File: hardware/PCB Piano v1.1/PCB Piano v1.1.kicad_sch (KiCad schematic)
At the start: 0 parts

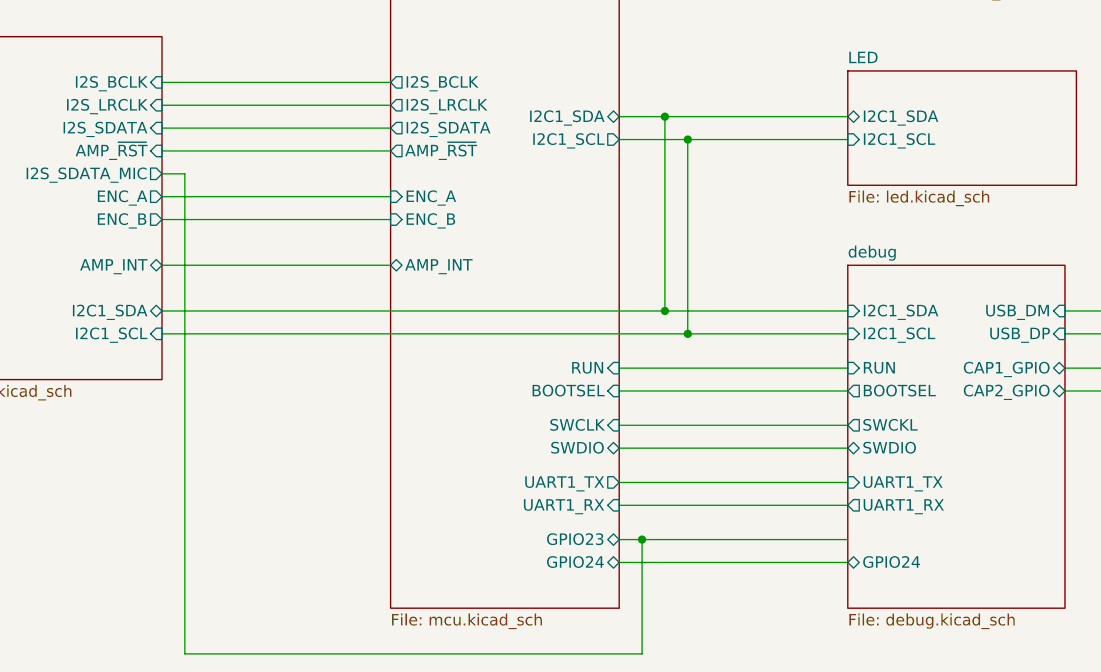
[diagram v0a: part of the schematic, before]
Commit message: Development Phase - PCB Complete - ERC/DRC in progress
Development commit. PBC layout complete. ERC/DRC checks in progress. Swapped some connectors for JST connectors with Adafruit-style polarization.
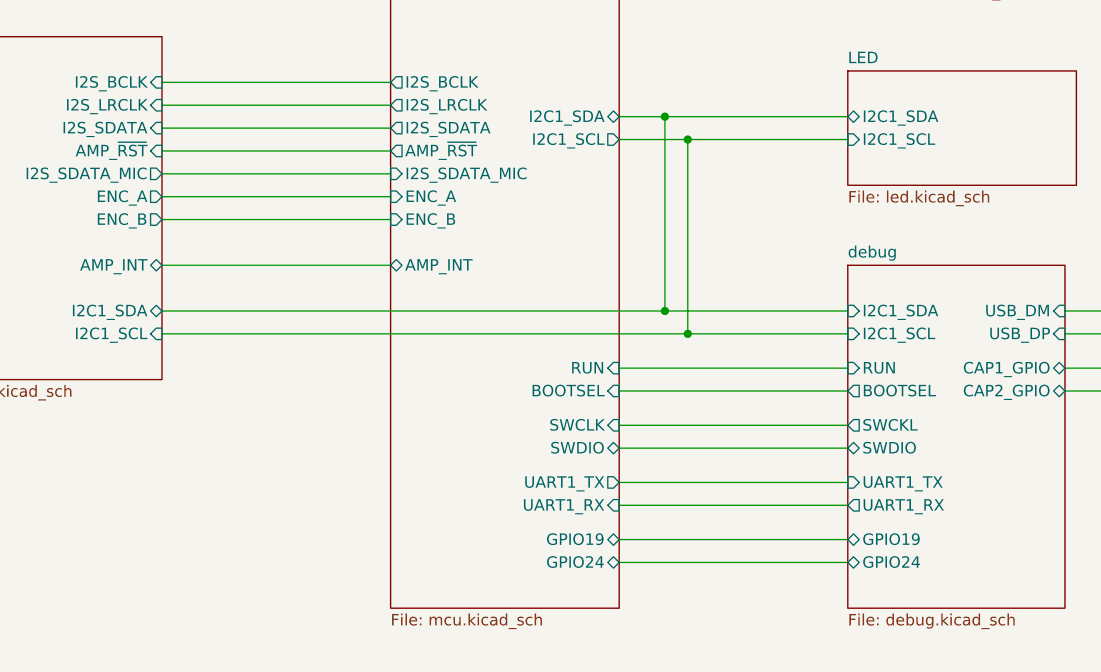
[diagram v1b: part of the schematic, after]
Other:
- sheet MCU ports: added GPIO19, I2S_SDATA_MIC; removed GPIO23
- sheet debug ports: added GPIO19; removed none
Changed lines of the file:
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@@
 		(color 0 0 0 0)
 	)
-	(junction
-		(at 154.94 151.13)
-		(diameter 0)
-		(color 0 0 0 0)
-	)
 	(wire
 		(pts
@@
 	(wire
 		(pts
-			(xy 104.14 163.83) (xy 104.14 110.49)
-		)
-		(stroke
-			(width 0)
-			(type default)
-		)
-	)
-	(wire
-		(pts
 			(xy 101.6 82.55) (xy 127 82.55)
 		)
@@
 	(wire
 		(pts
-			(xy 154.94 151.13) (xy 177.8 151.13)
+			(xy 152.4 151.13) (xy 177.8 151.13)
 		)
 		(stroke
@@
 	(wire
 		(pts
-			(xy 154.94 163.83) (xy 104.14 163.83)
-		)
-		(stroke
-			(width 0)
-			(type default)
-		)
-	)
-	(wire
-		(pts
 			(xy 101.6 64.77) (xy 121.92 64.77)
 		)
@@
 	(wire
 		(pts
-			(xy 152.4 151.13) (xy 154.94 151.13)
-		)
-		(stroke
-			(width 0)
-			(type default)
-		)
-	)
-	(wire
-		(pts
 			(xy 152.4 64.77) (xy 177.8 64.77)
 		)
@@
 	(wire
 		(pts
-			(xy 154.94 151.13) (xy 154.94 163.83)
-		)
-		(stroke
-			(width 0)
-			(type default)
-		)
-	)
-	(wire
-		(pts
 			(xy 207.01 132.08) (xy 207.01 73.66)
 		)
@@
 	(wire
 		(pts
-			(xy 104.14 110.49) (xy 101.6 110.49)
-		)
-		(stroke
-			(width 0)
-			(type default)
-		)
-	)
-	(wire
-		(pts
 			(xy 212.09 125.73) (xy 212.09 48.26)
 		)
@@
 		(pts
 			(xy 208.28 134.62) (xy 201.93 134.62)
+		)
+		(stroke
+			(width 0)
+			(type default)
+		)
+	)
+	(wire
+		(pts
+			(xy 101.6 110.49) (xy 127 110.49)
 		)
 		(stroke
@@
 			)
 		)
+		(pin "GPIO19" bidirectional
+			(at 177.8 151.13 180)
+			(effects
+				(font
+					(size 1.27 1.27)
+				)
+				(justify left)
+			)
+		)
 		(instances
 			(project "PCB Piano v1.1"
@@
 			)
 		)
-		(pin "GPIO23" bidirectional
-			(at 152.4 151.13 0)
-			(effects
-				(font
-					(size 1.27 1.27)
-				)
-				(justify right)
-			)
-		)
 		(pin "BOOTSEL" input
 			(at 152.4 134.62 0)
@@
 			)
 		)
+		(pin "GPIO19" bidirectional
+			(at 152.4 151.13 0)
+			(effects
+				(font
+					(size 1.27 1.27)
+				)
+				(justify right)
+			)
+		)
+		(pin "I2S_SDATA_MIC" input
+			(at 127 110.49 180)
+			(effects
+				(font
+					(size 1.27 1.27)
+				)
+				(justify left)
+			)
+		)

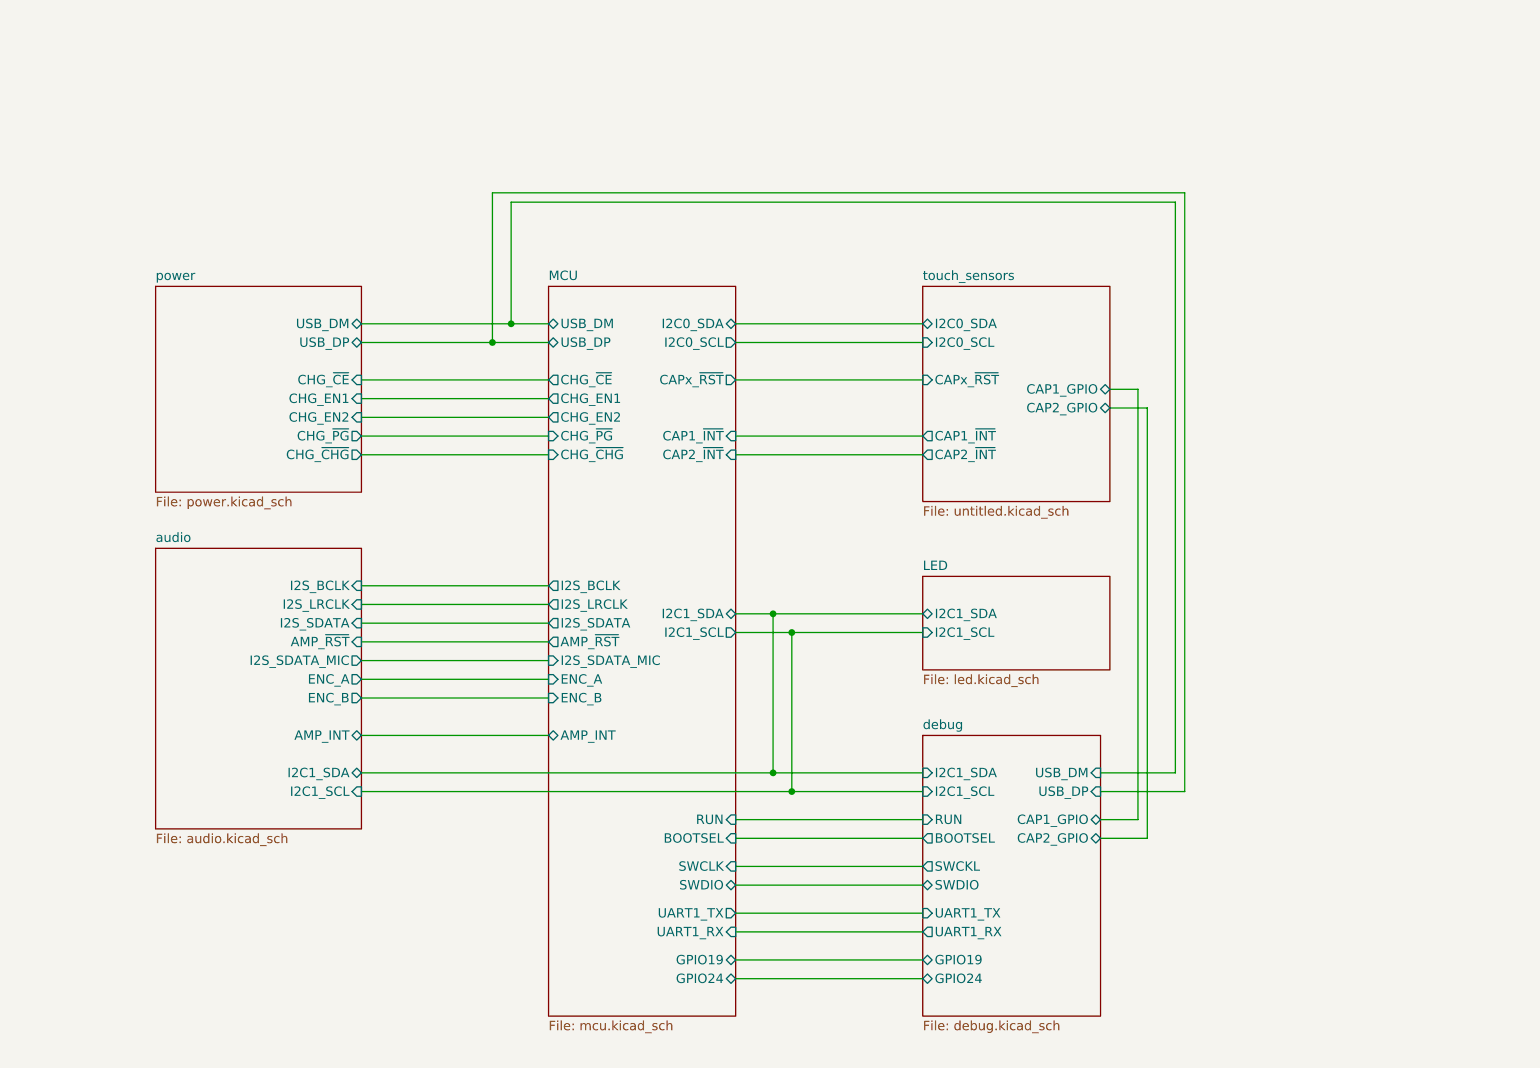
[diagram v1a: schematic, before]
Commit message: Firmware architecture complete - PCB revision with new charger.
Firmware Architecture Complete

- Added MP2724 charger driver
- Added TLV320DAC3100 driver
- Added MTCH2120 touch driver
- Added PCA9685 driver
- Added DotStar driver
- Added rotary encoder driver
- Added touch and LED maps
- Added control/audio/voice managers
- Added audio command queue
- Added Core1 audio architecture
- Added status LED system
- Added LED animation framework

Changes hardware schematic and PCB to accommodate a newer-style USB-C sink battery charger chip and USB data MUX to protect MCU while powered off.
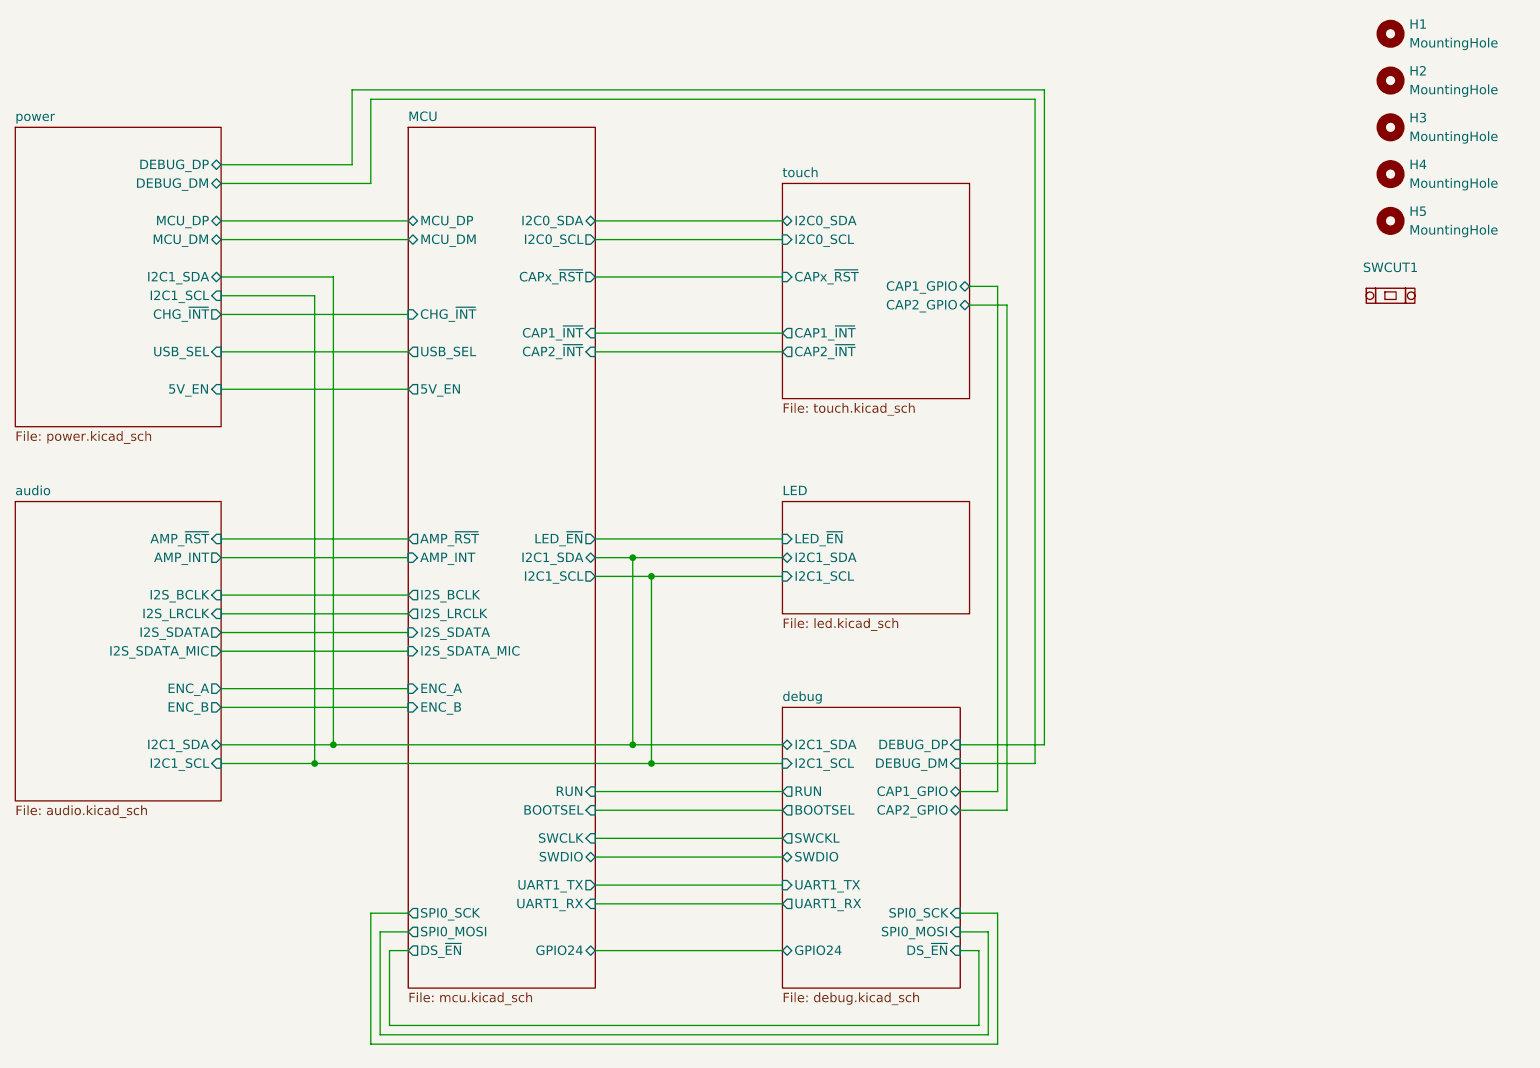
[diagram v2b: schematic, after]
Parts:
- added H1, H2, H3, H4, H5: MountingHole, MountingHole:MountingHole_3.2mm_M3, symbol Mechanical:MountingHole
- added SWCUT1: (no value), PCBPiano_Footprints:Switch_Slide_MFS126E_PanelCutout, symbol PCB_Piano_Symbols:Switch_Slide_MFS126E_PanelCutout
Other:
- sheet touch_sensors renamed touch
- sheet LED ports: added LED_~{EN}; removed none
- sheet MCU ports: added 5V_EN, CHG_~{INT}, DS_~{EN}, LED_~{EN}, MCU_DM, MCU_DP, SPI0_MOSI, SPI0_SCK, USB_SEL; removed CHG_EN1, CHG_EN2, CHG_~{CE}, CHG_~{CHG}, CHG_~{PG}, GPIO19, USB_DM, USB_DP
- sheet debug ports: added DEBUG_DM, DEBUG_DP, DS_~{EN}, SPI0_MOSI, SPI0_SCK; removed GPIO19, USB_DM, USB_DP
- sheet power ports: added 5V_EN, CHG_~{INT}, DEBUG_DM, DEBUG_DP, I2C1_SCL, I2C1_SDA, MCU_DM, MCU_DP, USB_SEL; removed CHG_EN1, CHG_EN2, CHG_~{CE}, CHG_~{CHG}, CHG_~{PG}, USB_DM, USB_DP
- sheet touch: file untitled.kicad_sch -> touch.kicad_sch

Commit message: PCB Finalized and Ordered. Firmware near completion.
PCB Finalized and Ordered. Final revisions included fixing bugs on some peripheral chips. Also added an RTC circuit after realizing the SD card could benefit from adding file timestamps.

Firmware near completion. Still need to finalize some SD card operations. Synth audio core is finished and all the board peripheral chip drivers were completed.
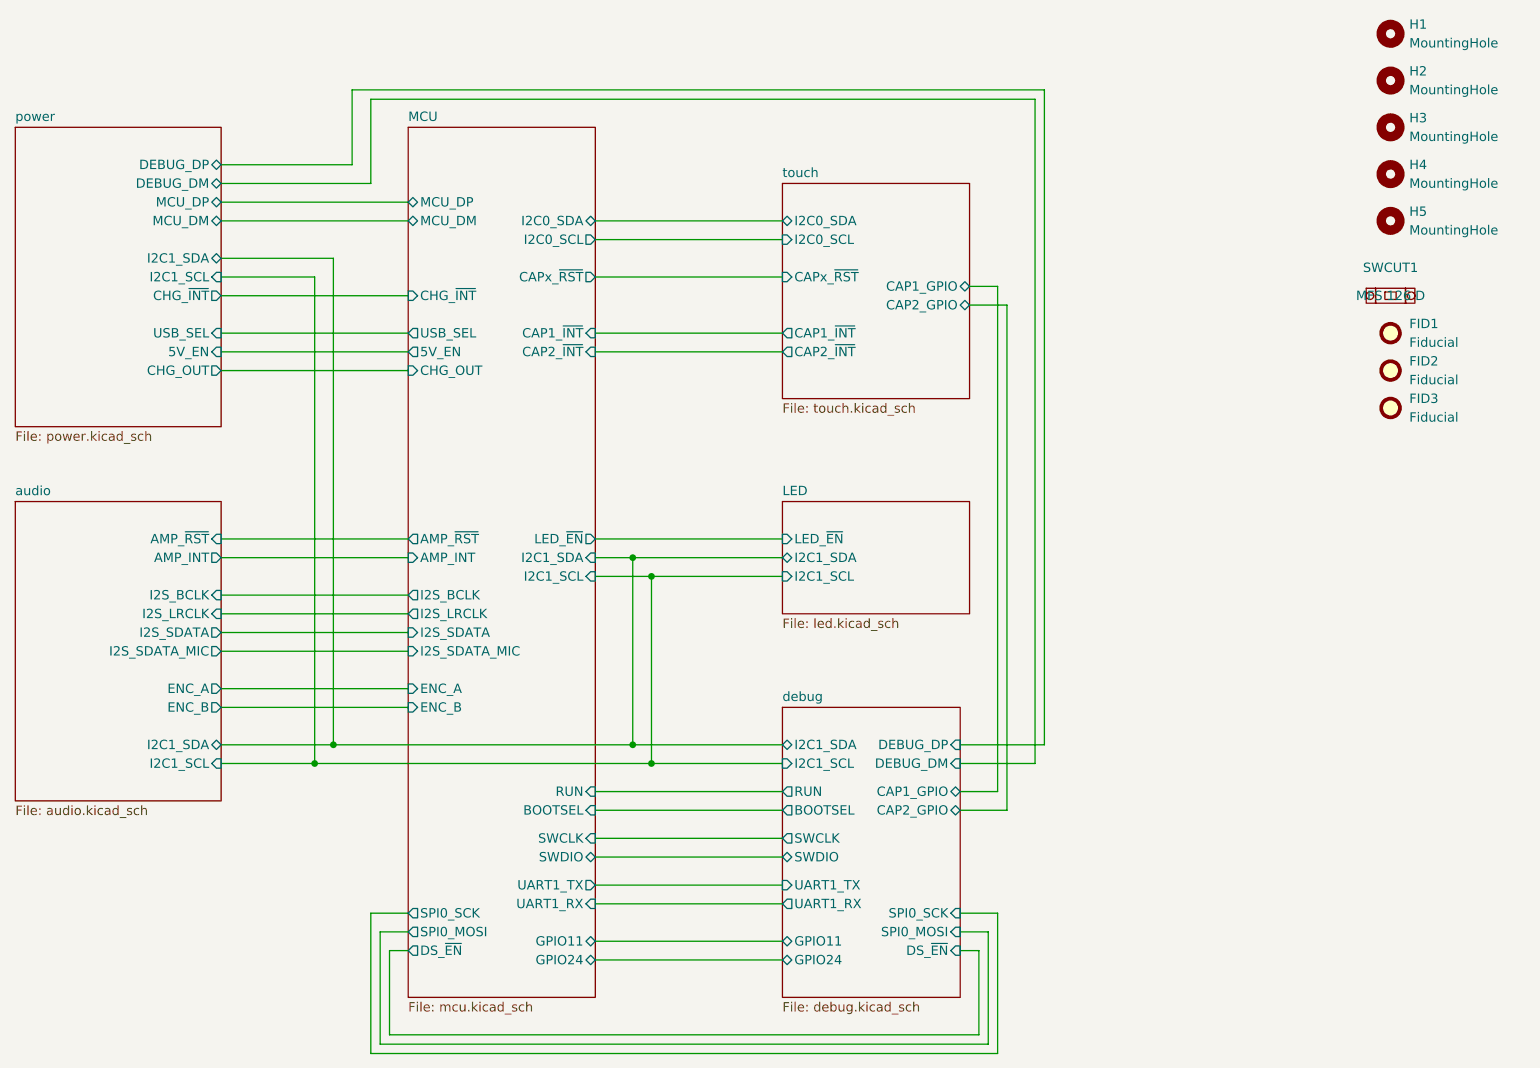
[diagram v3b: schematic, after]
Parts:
- added FID1, FID2, FID3: Fiducial, Fiducial:Fiducial_1mm_Mask3mm, symbol Mechanical:Fiducial
- SWCUT1: value (none) -> MFS 126 D; DigiKey_Part_Number (none) -> MFS 126 D; Manufacturer Part Number (none) -> MFS 126 D
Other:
- sheet MCU ports: added CHG_OUT, GPIO11; removed none
- sheet debug ports: added GPIO11, SWCLK; removed SWCKL
- sheet power ports: added CHG_OUT; removed none
